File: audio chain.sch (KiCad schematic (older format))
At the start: 32 parts, among them IC1 LM2902AWYDT, IC2 LM2902AWYDT, Q1 Q_NPN_BCE, Q2 Q_PNP_BCE, Q3 Q_NPN_BCE, Q4 Q_PNP_BCE

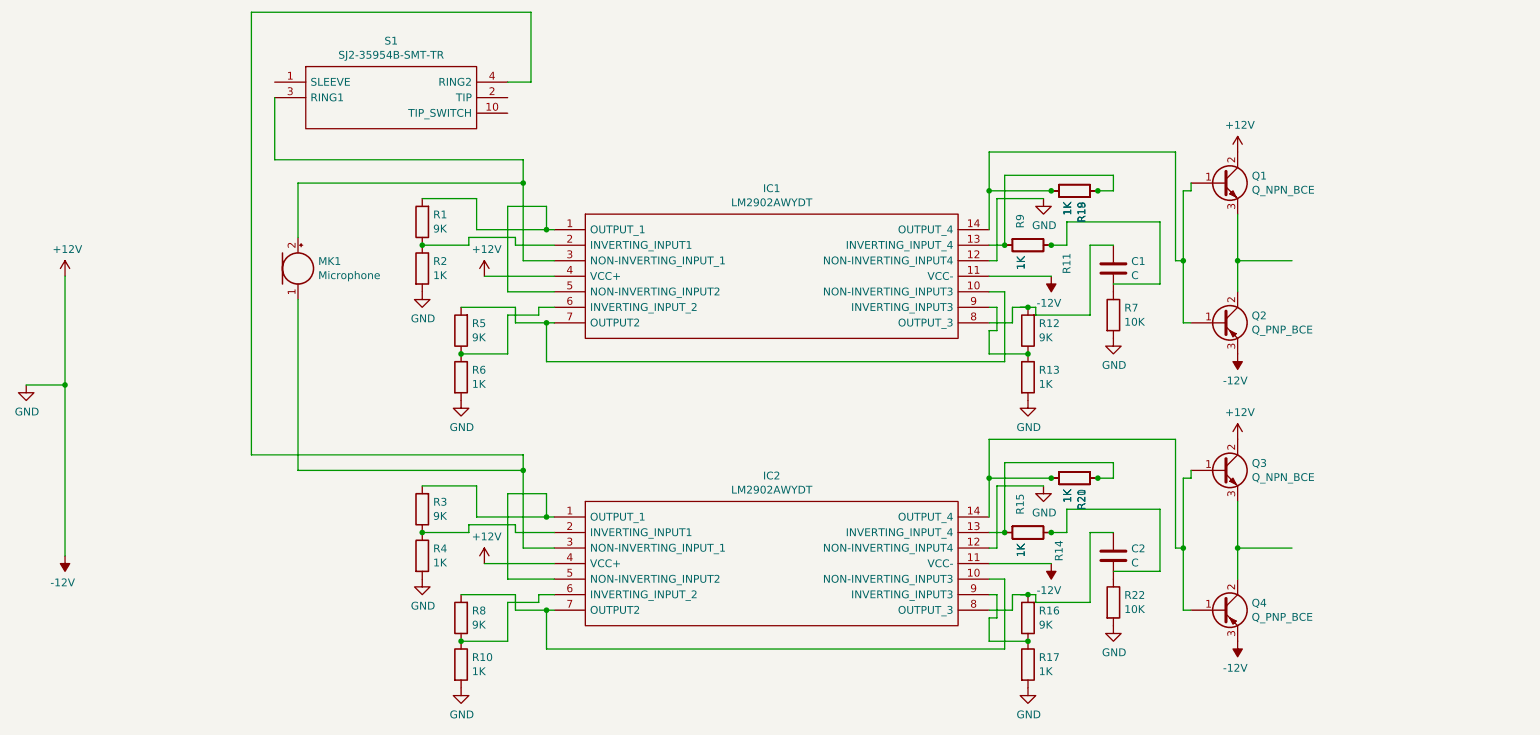
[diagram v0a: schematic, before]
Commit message: added transistor footprint
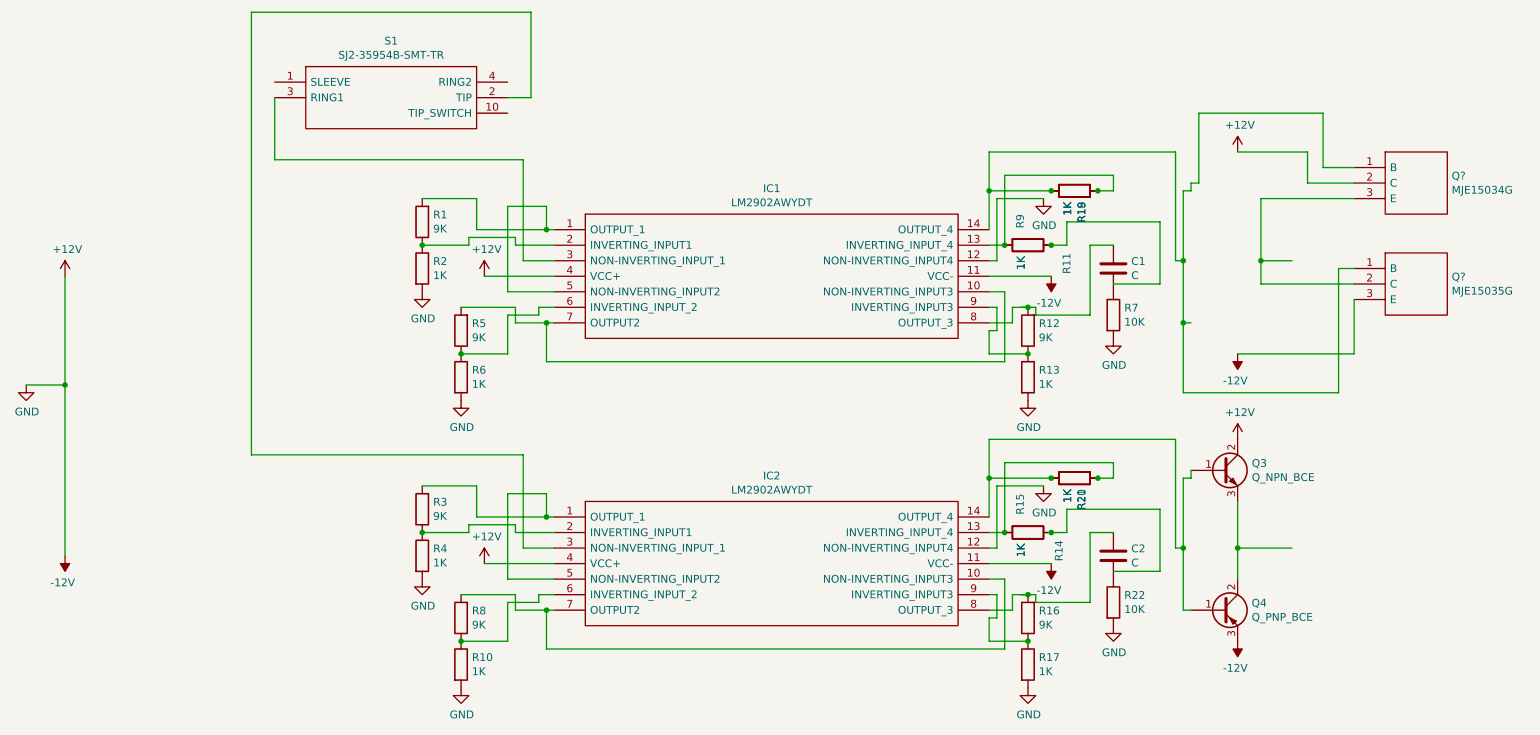
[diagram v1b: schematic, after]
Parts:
- removed MK1: Microphone, symbol Device:Microphone
- removed Q1: Q_NPN_BCE, symbol Device:Q_NPN_BCE
- removed Q2: Q_PNP_BCE, symbol Device:Q_PNP_BCE
- added Q?: MJE15034G, TO254P483X1010X2035-3P, symbol SamacSys_Parts:MJE15034G
- added Q?: MJE15035G, TO254P483X1010X2035-3P, symbol SamacSys_Parts:MJE15035G
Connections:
- wire segments 158 -> 168
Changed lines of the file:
@@
 Connection ~ 1400 3550
-$Comp
-L Device:Microphone MK1
-U 1 1 613E6E32
-P 2900 2800
-F 0 "MK1" H 3030 2846 50  0000 L CNN
-F 1 "Microphone" H 3030 2755 50  0000 L CNN
-F 2 "" V 2900 2900 50  0001 C CNN
-F 3 "~" V 2900 2900 50  0001 C CNN
-	1    2900 2800
-	1    0    0    -1
-$EndComp
 $Comp
 L power:-12V #PWR0107
@@
 $EndComp
 $Comp
-L Device:Q_NPN_BCE Q1
-U 1 1 617DDDC3
-P 8850 2250
-F 0 "Q1" H 9041 2296 50  0000 L CNN
-F 1 "Q_NPN_BCE" H 9041 2205 50  0000 L CNN
-F 2 "" H 9050 2350 50  0001 C CNN
-F 3 "~" H 8850 2250 50  0001 C CNN
-	1    8850 2250
-	1    0    0    -1
-$EndComp
-$Comp
-L Device:Q_PNP_BCE Q2
-U 1 1 617DEF87
-P 8850 3150
-F 0 "Q2" H 9040 3196 50  0000 L CNN
-F 1 "Q_PNP_BCE" H 9040 3105 50  0000 L CNN
-F 2 "" H 9050 3250 50  0001 C CNN
-F 3 "~" H 8850 3150 50  0001 C CNN
-	1    8850 3150
-	1    0    0    -1
-$EndComp
-$Comp
 L power:-12V #PWR0117
 U 1 1 617DFF4A
@@
 	8600 3150 8650 3150
 Wire Wire Line
-	8950 2450 8950 2750
-Wire Wire Line
-	9300 2750 8950 2750
-Connection ~ 8950 2750
-Wire Wire Line
-	8950 2750 8950 2950
+	9300 2750 9100 2750
 $Comp
 L power:+12V #PWR0104
@@
 	8600 2300 8600 2750
 Wire Wire Line
-	2900 2600 2900 2250
-Wire Wire Line
-	2900 2250 4350 2250
-Wire Wire Line
-	4350 2250 4350 2750
-Wire Wire Line
 	4350 2750 4550 2750
 Wire Wire Line
@@
 	8600 4150 8600 4600
 Wire Wire Line
-	4350 4100 4350 4600
-Wire Wire Line
 	4350 4600 4550 4600
 Wire Wire Line
@@
 Wire Wire Line
 	8600 4600 8600 5000
-Wire Wire Line
-	2900 3000 2900 4100
-Wire Wire Line
-	2900 4100 4350 4100
 Wire Wire Line
 	7550 3050 7600 3050
@@
 	2750 2100 4350 2100
 Wire Wire Line
-	4350 2100 4350 2250
-Connection ~ 4350 2250
-Wire Wire Line
-	4250 1600 4400 1600
-Wire Wire Line
-	4400 1600 4400 1150
-Wire Wire Line
 	4400 1150 2600 1150
 Wire Wire Line
@@
 	2600 4000 4350 4000
 Wire Wire Line
-	4350 4000 4350 4100
-Connection ~ 4350 4100
+	4250 1700 4400 1700
+Wire Wire Line
+	4400 1150 4400 1700
+$Comp
+L SamacSys_Parts:MJE15034G Q?
+U 1 1 61ACC405
+P 9700 2150
+F 0 "Q?" H 10328 2096 50  0000 L CNN
+F 1 "MJE15034G" H 10328 2005 50  0000 L CNN
+F 2 "TO254P483X1010X2035-3P" H 10350 2250 50  0001 L CNN
+F 3 "http://www.onsemi.com/pub/Collateral/MJE15034-D.PDF" H 10350 2150 50  0001 L CNN
+F 4 "" H 10350 2050 50  0001 L CNN "Description"
+F 5 "4.83" H 10350 1950 50  0001 L CNN "Height"
+F 6 "ON Semiconductor" H 10350 1850 50  0001 L CNN "Manufacturer_Name"
+F 7 "MJE15034G" H 10350 1750 50  0001 L CNN "Manufacturer_Part_Number"
+F 8 "863-MJE15034G" H 10350 1650 50  0001 L CNN "Mouser Part Number"
+F 9 "https://www.mouser.co.uk/ProductDetail/onsemi/MJE15034G?qs=HVbQlW5zcXV7QTziNO9oMQ%3D%3D" H 10350 1550 50  0001 L CNN "Mouser Price/Stock"
+F 10 "MJE15034G" H 10350 1450 50  0001 L CNN "Arrow Part Number"
+F 11 "https://www.arrow.com/en/products/mje15034g/on-semiconductor?region=europe" H 10350 1350 50  0001 L CNN "Arrow Price/Stock"
+	1    9700 2150
+	1    0    0    -1
+$EndComp
+$Comp
+L SamacSys_Parts:MJE15035G Q?
+U 1 1 61ACD380
+P 9700 2800
+F 0 "Q?" H 10328 2746 50  0000 L CNN
+F 1 "MJE15035G" H 10328 2655 50  0000 L CNN
+F 2 "TO254P483X1010X2035-3P" H 10350 2900 50  0001 L CNN
+F 3 "http://www.onsemi.com/pub/Collateral/MJE15034-D.PDF" H 10350 2800 50  0001 L CNN
+F 4 "" H 10350 2700 50  0001 L CNN "Description"
+F 5 "4.83" H 10350 2600 50  0001 L CNN "Height"
+F 6 "ON Semiconductor" H 10350 2500 50  0001 L CNN "Manufacturer_Name"
+F 7 "MJE15035G" H 10350 2400 50  0001 L CNN "Manufacturer_Part_Number"
+F 8 "863-MJE15035G" H 10350 2300 50  0001 L CNN "Mouser Part Number"
+F 9 "https://www.mouser.co.uk/ProductDetail/onsemi/MJE15035G?qs=HVbQlW5zcXXa%252Byhv1vIoqQ%3D%3D" H 10350 2200 50  0001 L CNN "Mouser Price/Stock"
+F 10 "MJE15035G" H 10350 2100 50  0001 L CNN "Arrow Part Number"
+F 11 "https://www.arrow.com/en/products/mje15035g/on-semiconductor?region=europe" H 10350 2000 50  0001 L CNN "Arrow Price/Stock"
+	1    9700 2800
+	1    0    0    -1
+$EndComp
+Wire Wire Line
+	8700 2250 8700 1800
+Wire Wire Line
+	8700 1800 9500 1800
+Wire Wire Line
+	9500 1800 9500 2150
+Wire Wire Line
+	9500 2150 9700 2150
+Wire Wire Line
+	8950 2050 9400 2050
+Wire Wire Line
+	9400 2050 9400 2250
+Wire Wire Line
+	9400 2250 9700 2250
+Wire Wire Line
+	9700 2350 9100 2350
+Wire Wire Line
+	9100 2350 9100 2750
+Connection ~ 9100 2750
+Wire Wire Line
+	9100 2750 9100 2900
+Wire Wire Line
+	9100 2900 9700 2900
+Wire Wire Line
+	8600 3150 8600 3600
+Wire Wire Line
+	8600 3600 9600 3600
+Wire Wire Line
+	9600 3600 9600 2800
+Wire Wire Line
+	9600 2800 9700 2800
+Connection ~ 8600 3150
+Wire Wire Line
+	9700 3000 9700 3350
+Wire Wire Line
+	9700 3350 8950 3350
+Wire Wire Line
+	8650 2250 8700 2250
+Wire Wire Line
+	4350 2100 4350 2750
+Wire Wire Line
+	4350 4000 4350 4600
 $EndSCHEMATC
